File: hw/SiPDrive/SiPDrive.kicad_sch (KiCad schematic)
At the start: 87 parts, among them Q1 CMSA015N06, Q2 CMSA015N06, Q3 CMSA015N06, Q4 CMSA015N06, Q5 CMSA015N06, Q6 CMSA015N06, U1 STSPIN32G4, U2 MT6701, U3 TCAN1057, U4 LDO, U5 SH-3P

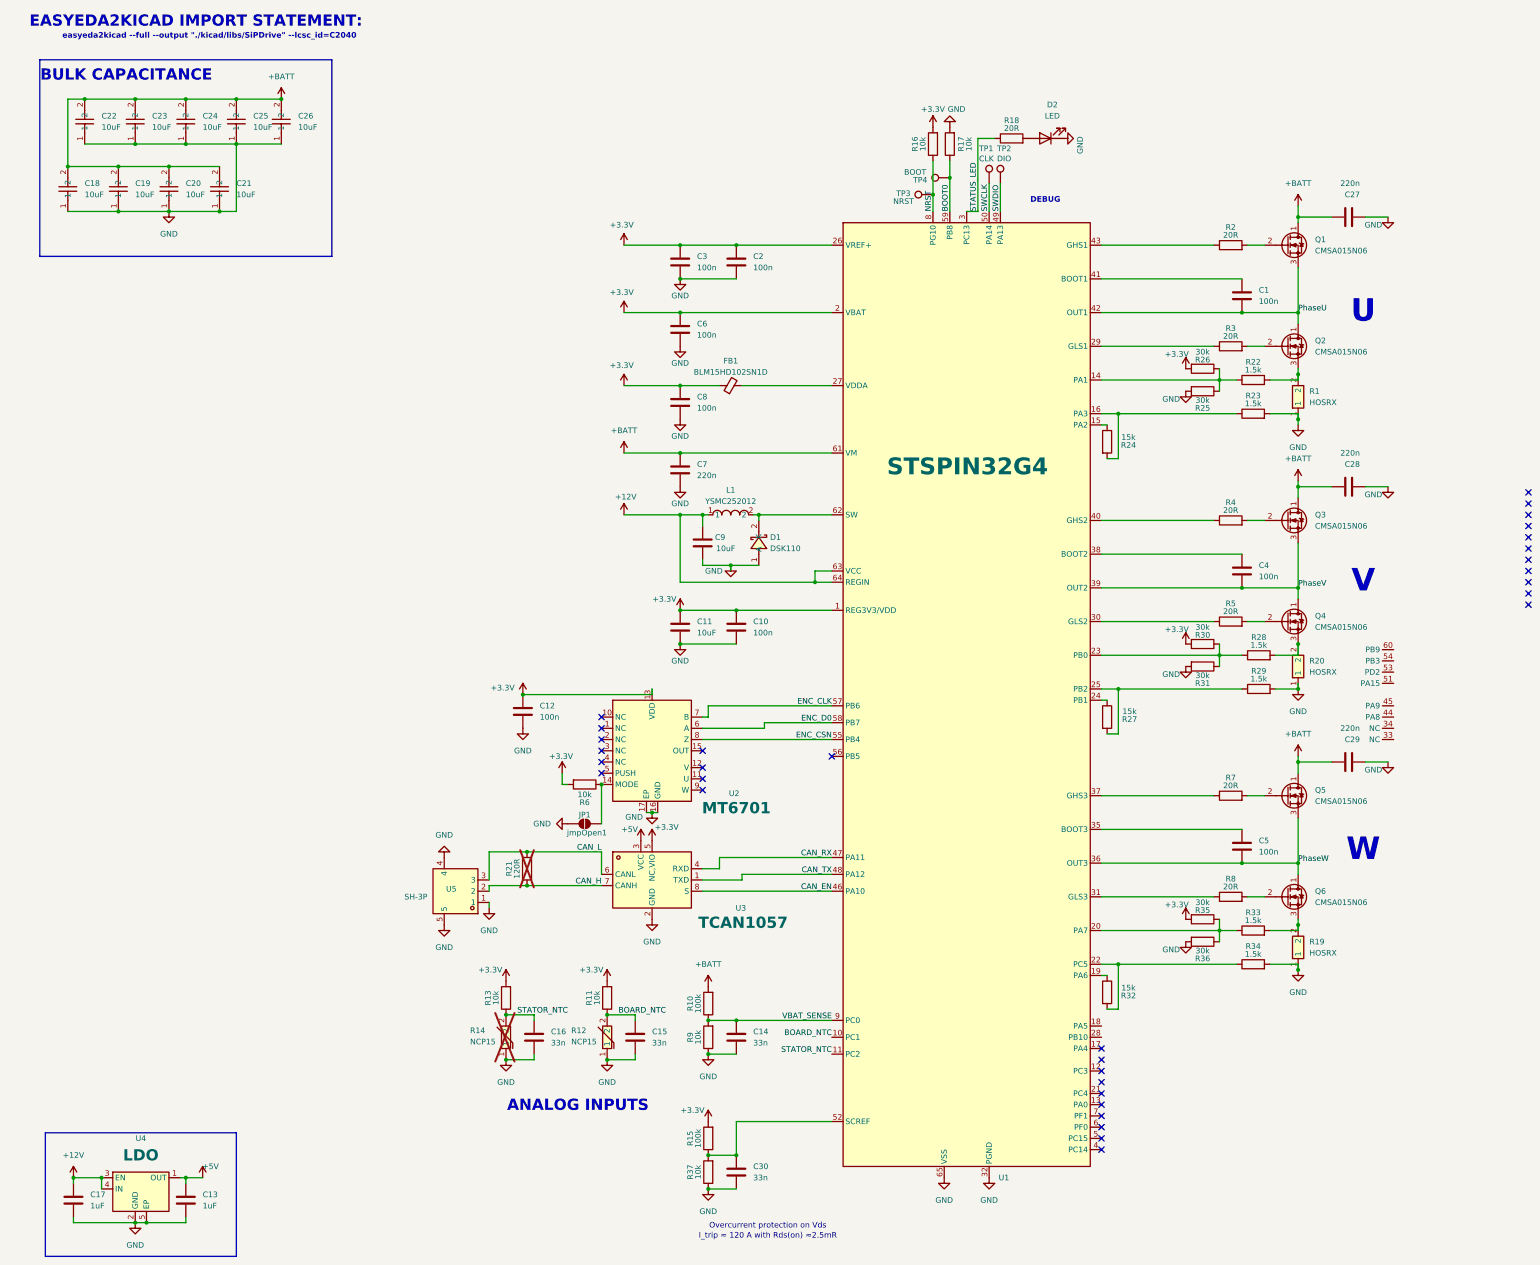
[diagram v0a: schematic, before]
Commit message: Updated schematic to a 3 shunt topology and made first deboard PCB layout
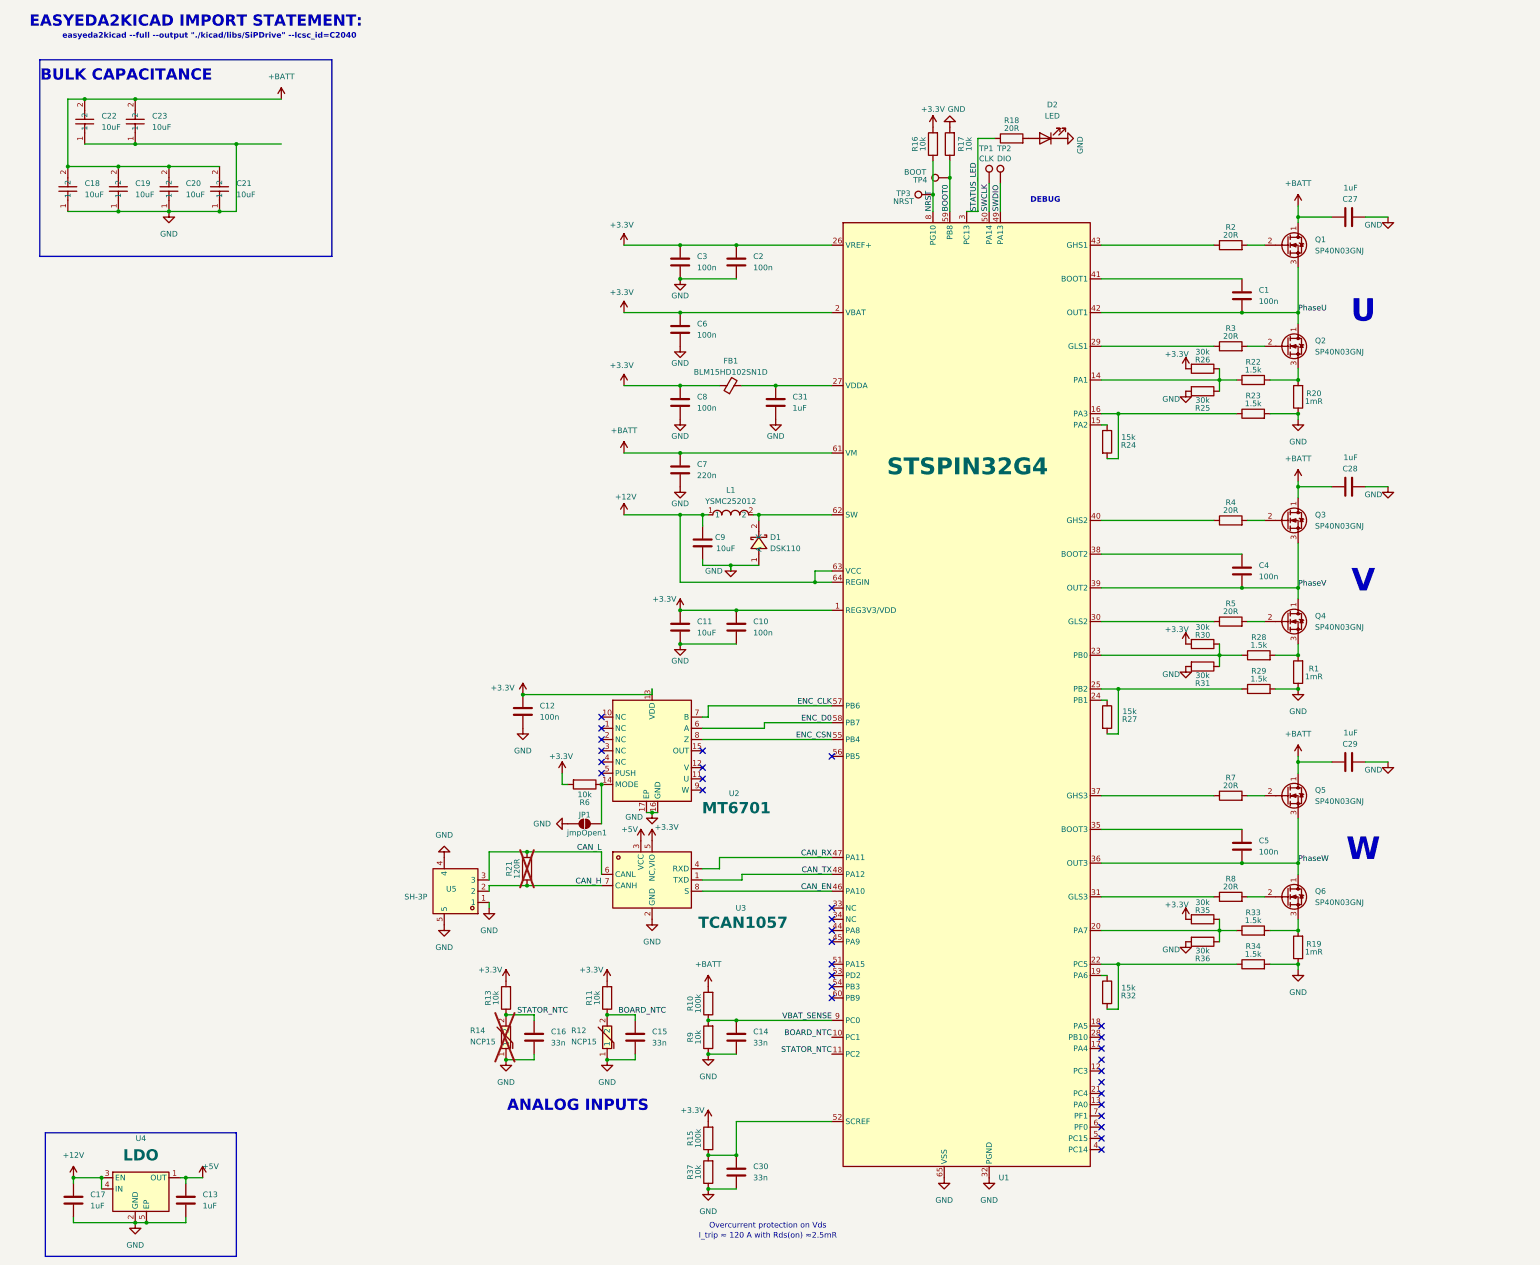
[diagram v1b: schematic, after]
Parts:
- removed C24, C25, C26: 10uF, SiPDrive:C1210, symbol SiPDrive:GRM32EC72A106KE05L
- removed R1, R19, R20: HOSRX, SiPDrive:RES-SMD_L3.2-W1.6_SR120620F0M50SZ, symbol SiPDrive:HOSRX1206-3W-1MR-1%
- added C31: 1uF, Capacitor_SMD:C_0603_1608Metric, symbol Device:C
- added R1, R19, R20: 1mR, Resistor_SMD:R_0805_2012Metric, symbol Device:R
- C13, C17: LCSC C14445 -> C52923
- C27, C28, C29: value 220n -> 1uF; footprint Capacitor_SMD:C_0603_1608Metric -> Capacitor_SMD:C_0402_1005Metric; LCSC C162178 -> C1518208
- Q1, Q2, Q3, Q4, Q5, Q6: value CMSA015N06 -> SP40N03GNJ; footprint SiPDrive:PDFN-8_L5.8-W5.0-P1.27-LS6.1-BL -> SiPDrive:POWERPAK-1212-8_L3.0-W3.0-P0.65-LS3.3-BL; LCSC C42428219 -> C22466709
- R10, R15: LCSC C114763 -> C25530
- R22, R23, R28, R29, R33, R34: LCSC C138031 -> C25867
- R24, R27, R32: LCSC C138031 -> C25756
- R25, R26, R30, R31, R35, R36: LCSC C138031 -> C25553
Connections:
- net GND: now also C31.2, R1.1, R19.1, R20.1
- net at Q4.3 (S), R28.2: now also R1.2
- net at Q2.3 (S), R22.2: now also R20.2
- net at Q6.3 (S), R33.2: now also R19.2
- net at FB1.2, U1.27 (VDDA): now also C31.1
- no-connect marks 32 -> 31
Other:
- moved on the sheet: U1

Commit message: Ordered first dev board and components
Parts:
- removed C3, C8: 100n, Capacitor_SMD:C_0402_1005Metric, symbol Device:C
- C31: footprint Capacitor_SMD:C_0603_1608Metric -> Capacitor_SMD:C_0402_1005Metric; LCSC (none) -> C14445
- C7: LCSC C162178 -> C21120
- JP1: footprint (none) -> Jumper:SolderJumper-2_P1.3mm_Open_RoundedPad1.0x1.5mm

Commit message: other shunts, redo routing
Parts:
- removed R1, R19, R20: 1mR, Resistor_SMD:R_0805_2012Metric, symbol Device:R
- removed R21: 120R, Resistor_SMD:R_0805_2012Metric, symbol Device:R
- added R1, R19, R21: SME08A1FR002T, SiPDrive:R0508, symbol SiPDrive:SME08A1FR002T
- added U6: SH-3P, SiPDrive:CONN-SMD_SM03B-SRSS-TB-LF-SN-P, symbol SiPDrive:SM03B-SRSS-TB(LF)(SN)(P)
- C1, C10, C12, C2, C4, C5, C6: footprint Capacitor_SMD:C_0402_1005Metric -> Capacitor_SMD:C_0201_0603Metric; LCSC C162178 -> C181043
- C14, C15, C16, C30: footprint Capacitor_SMD:C_0402_1005Metric -> Capacitor_SMD:C_0201_0603Metric; LCSC C106862 -> C161475
- C18, C19, C20, C21, C22, C23: footprint SiPDrive:C1210 -> Capacitor_SMD:C_1206_3216Metric; LCSC Part C576517 -> C5119295
- R10, R15: footprint Resistor_SMD:R_0402_1005Metric -> Resistor_SMD:R_0201_0603Metric; LCSC C25530 -> C270364
- R11, R13, R16, R17, R37, R6, R9: footprint Resistor_SMD:R_0402_1005Metric -> Resistor_SMD:R_0201_0603Metric; LCSC C60490 -> C473048
- R18, R2, R3, R4, R5, R7, R8: footprint Resistor_SMD:R_0402_1005Metric -> Resistor_SMD:R_0201_0603Metric; LCSC C138031 -> C473548
- R22, R23, R28, R29, R33, R34: footprint Resistor_SMD:R_0402_1005Metric -> Resistor_SMD:R_0201_0603Metric; LCSC C25867 -> C270361
- R24, R27, R32: footprint Resistor_SMD:R_0402_1005Metric -> Resistor_SMD:R_0201_0603Metric; LCSC C25756 -> C473452
- R25, R26, R30, R31, R35, R36: footprint Resistor_SMD:R_0402_1005Metric -> Resistor_SMD:R_0201_0603Metric; LCSC C25553 -> C246933
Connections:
- net CAN_H: now also U6.2
- net CAN_L: now also U6.3
- net GND: now also R1.1, R19.1, R21.1, U6.1, U6.4, U6.5
- net at Q4.3 (S), R28.2: now also R1.2
- net at Q2.3 (S), R22.2: now also R21.2
- net at Q6.3 (S), R33.2: now also R19.2
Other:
- moved on the sheet: U5

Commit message: started routing
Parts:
- added D3: SMBJ26A_C908802, SiPDrive:SMB_L4.5-W3.7-LS5.4-RD, symbol SiPDrive:SMBJ26A_C908802
- C7: footprint Capacitor_SMD:C_0603_1608Metric -> Capacitor_SMD:C_0402_1005Metric; LCSC C21120 -> C49333232
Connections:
- net +BATT: now also D3.1
- net GND: now also D3.2

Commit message: Final routing, code fixes, production files and BOM
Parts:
- removed C22, C23: 10uF, Capacitor_SMD:C_1206_3216Metric, symbol SiPDrive:GRM32EC72A106KE05L
- removed C6: 100n, Capacitor_SMD:C_0201_0603Metric, symbol Device:C
- added C24, C25, C26, C32, C33, C34, C35, C36, C37, C38, C6, C8: 10uF, Capacitor_SMD:C_1206_3216Metric, symbol SiPDrive:GRM32EC72A106KE05L
- added C3: 100n, Capacitor_SMD:C_0201_0603Metric, symbol Device:C
- added U7: ~, SiPDrive:SiPDrive_EDGE, symbol SiPDrive:SiPDrive_EDGE
- C18, C19, C20, C21: LCSC (none) -> C5119295; LCSC Part C5119295 -> (none)
- D1: LCSC (none) -> C908227; LCSC Part C908227 -> (none)
- D3: LCSC (none) -> C908802; LCSC Part C908802 -> (none)
- L1: LCSC (none) -> C41405922; LCSC Part C41405922 -> (none)
- R1, R19, R21: LCSC (none) -> C2692045; LCSC Part C2692045 -> (none)
- R12, R14: LCSC (none) -> C77131; LCSC Part C77131 -> (none)
- U1: LCSC (none) -> C7434864; LCSC Part C7434864 -> (none)
- U2: LCSC (none) -> C2913974; LCSC Part C2913974 -> (none)
- U3: LCSC (none) -> C3236208; LCSC Part C3236208 -> (none)
- U4: LCSC (none) -> C39673733; LCSC Part C39673733 -> (none)
- U5, U6: LCSC (none) -> C160403; LCSC Part C160403 -> (none)
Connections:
- net +3.3V: now also C3.1
- net +BATT: now also C24.2, C25.2, C26.2, C32.2, C33.2, C34.2, C35.2, C36.2, C37.2, C38.2, C6.2, C8.2, U7.4 (V+)
- net GND: now also C24.1, C25.1, C26.1, C3.2, C32.1, C33.1, C34.1, C35.1, C36.1, C37.1, C38.1, C6.1, C8.1, U7.5 (V-)
- net PhaseU: now also U7.3 (C)
- net PhaseV: now also U7.1 (A)
- net PhaseW: now also U7.2 (B)
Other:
- moved on the sheet: C18, C19, C20, C21, D3
